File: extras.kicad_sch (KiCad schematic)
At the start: 4 parts

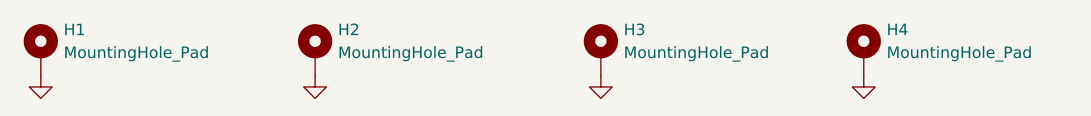
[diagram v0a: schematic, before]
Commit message: replace flash memory with SD flash memory; move SPI2 terminations closer to source
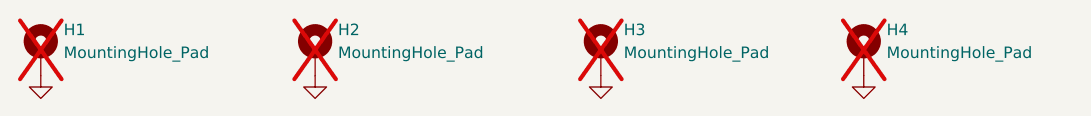
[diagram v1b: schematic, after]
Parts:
- H1, H2, H3, H4: now not fitted
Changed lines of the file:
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@@
 		(in_bom yes)
 		(on_board yes)
-		(dnp no)
+		(dnp yes)
 		(fields_autoplaced yes)
 		(property "Reference" "H2"
@@
 		(in_bom yes)
 		(on_board yes)
-		(dnp no)
+		(dnp yes)
 		(fields_autoplaced yes)
 		(property "Reference" "H3"
@@
 		(in_bom yes)
 		(on_board yes)
-		(dnp no)
+		(dnp yes)
 		(fields_autoplaced yes)
 		(property "Reference" "H1"
@@
 		(in_bom yes)
 		(on_board yes)
-		(dnp no)
+		(dnp yes)
 		(fields_autoplaced yes)
 		(property "Reference" "H4"
